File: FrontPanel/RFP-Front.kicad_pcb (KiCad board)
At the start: 2 copper layers, 106 x 56.6 mm, 21 parts, among them J1 COMM, J2 SWD, J3 BUZZ / BTNLED, U1 STM32F103C8T6, U2 OLED_128x64

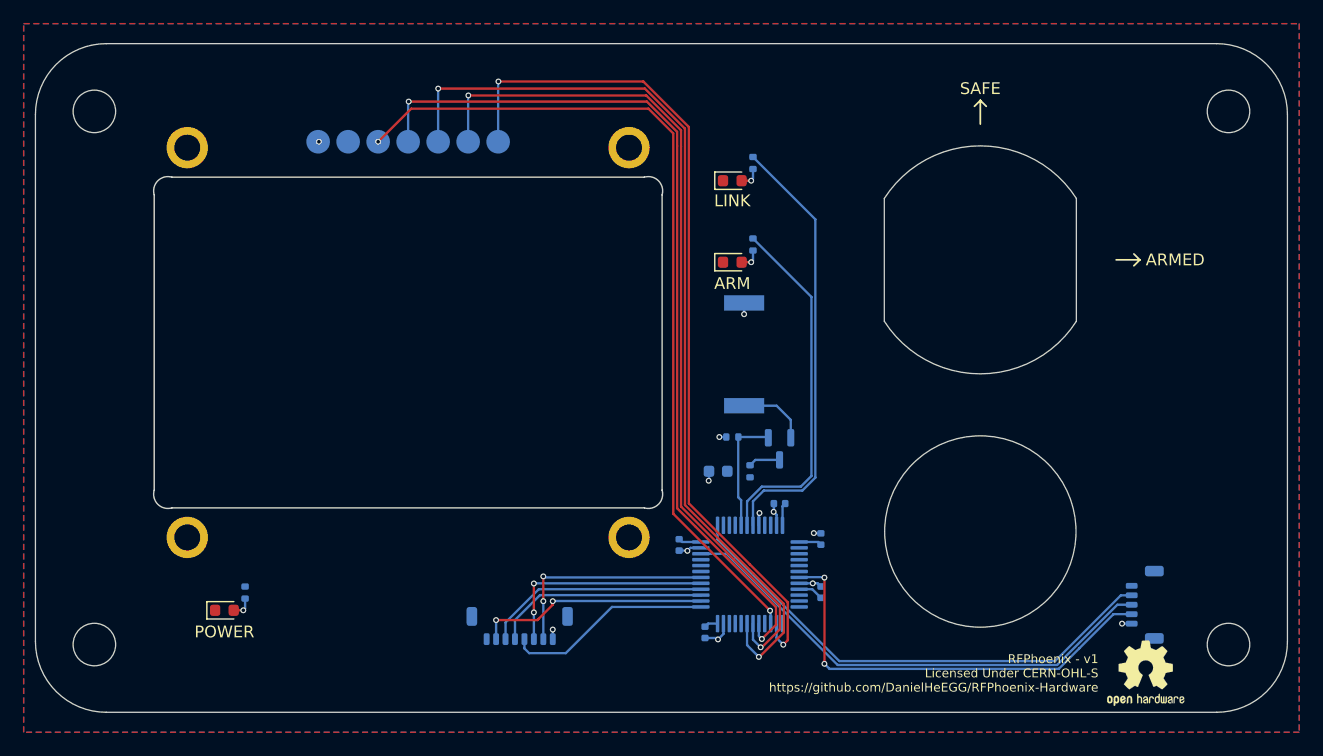
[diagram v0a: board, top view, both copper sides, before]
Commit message: Rearrange OLED and connector for front panel
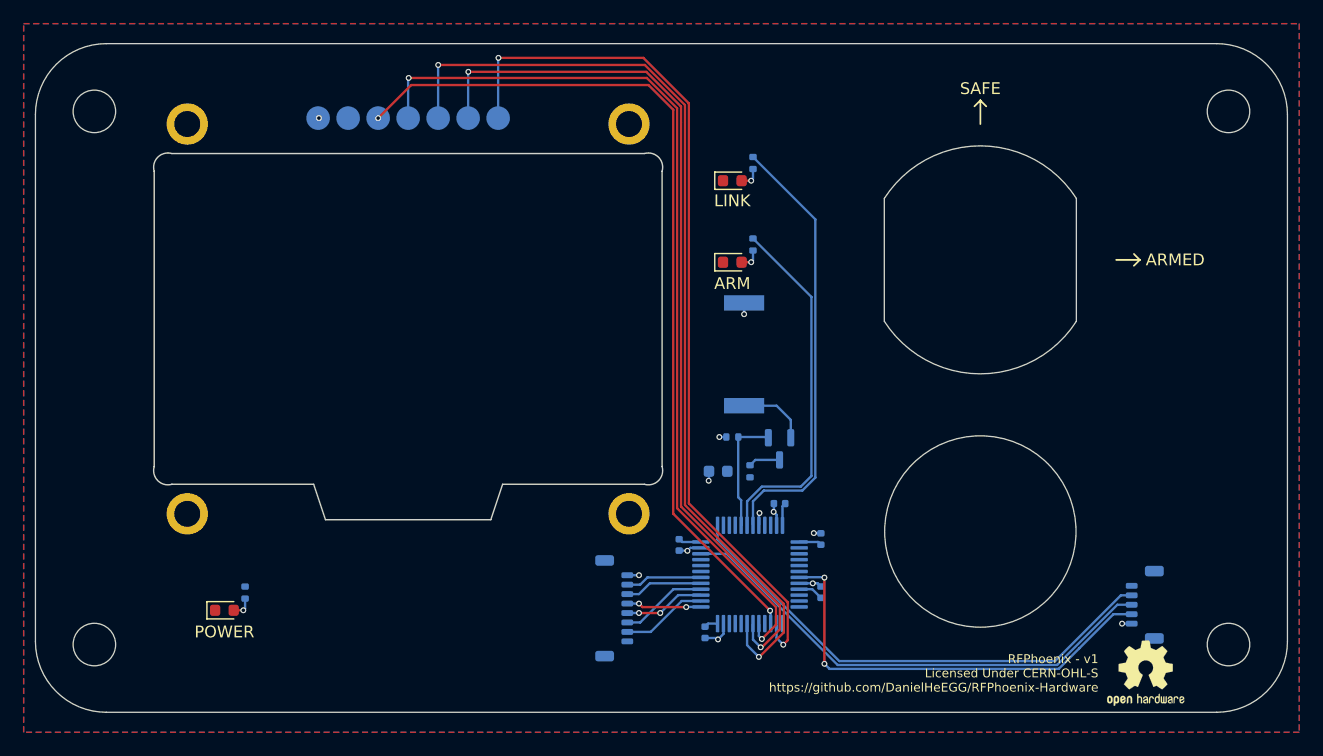
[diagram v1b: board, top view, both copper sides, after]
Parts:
- moved J1 8.14 mm to (-4.00, 19.5), turned to 90 degrees
- moved U2 2.00 mm to (-21.4, -5.00)
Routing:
- net COMM_SCK: track 19.8 -> 7.31 mm, vias 2 -> 0
- net COMM_RFU1: track 18.9 -> 6.61 mm, vias 2 -> 0
- net COMM_RFU2: track 18.7 -> 6.48 mm, vias 2 -> 0
- net COMM_MOSI: track 19.1 -> 7.39 mm
- net COMM_MISO: track 18.2 -> 6.86 mm, vias 0 -> 2
- net COMM_nCS: track 17.5 -> 6.36 mm, vias 0 -> 2
- net OLED_nCS: track 72.3 -> 74.3 mm
- net OLED_nRST: track 79.1 -> 81.1 mm
- net OLED_SCK: track 71.9 -> 73.9 mm
- net OLED_DC: track 73.4 -> 75.4 mm
- net OLED_MOSI: track 75.5 -> 77.5 mm

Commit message: Rearrange and dim LEDs
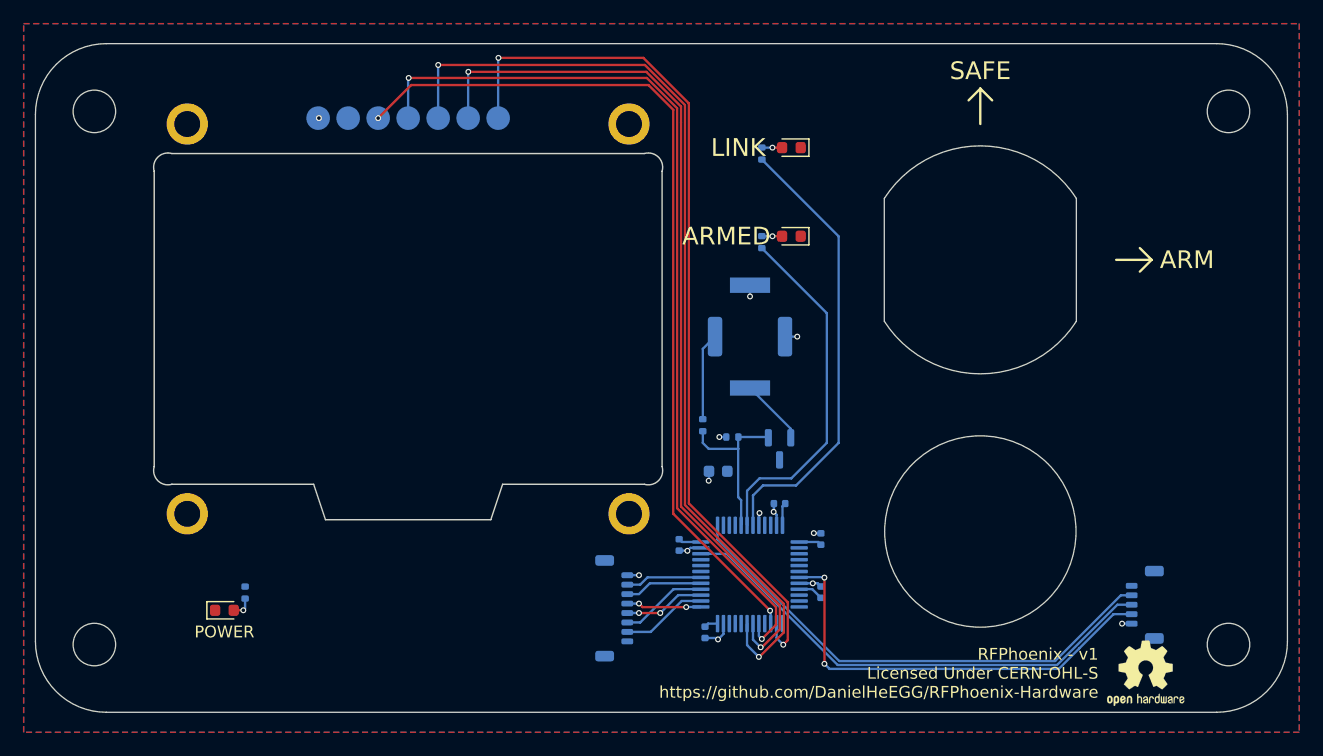
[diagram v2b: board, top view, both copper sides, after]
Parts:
- added J4: LED_LIVE, Resistor_SMD:R_2512_6332Metric, B.Cu at (7.50, -3.50)
- J3: value BUZZ / BTNLED -> BUZZER
- R1, R2: value 100 -> 470R
- R3: value 100 -> 100R
- R5: value 33 -> 100R
- moved D2 5.73 mm to (11.0, -19.5), turned to 180 degrees
- moved R5 5.59 mm to (3.50, 4.00)
- moved D3 5.46 mm to (11.0, -12.0), turned to 180 degrees
- moved J3 1.58 mm to (7.50, -3.50)
- moved R2 1.10 mm to (8.50, -19.0), turned to 90 degrees
- moved R3 0.78 mm to (8.50, -11.5), turned to 90 degrees
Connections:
- Q1 pad 3: Net-(Q1-Pad3) -> +3.3V
- R5 pad 1: +3.3V -> LED_LIVE
- R5 pad 2: Net-(Q1-Pad3) -> Net-(R5-Pad2)
- U1 pad 40: unconnected-(U1-Pad40) -> LED_CONT
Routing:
- net Net-(R5-Pad2): track 0.00 -> 7.42 mm
- net LED_LIVE: track 10.1 -> 14.3 mm
- net Net-(Q1-Pad3): track 2.69 -> 0.00 mm
- net GND: track 14.3 -> 15.4 mm, vias 12 -> 13
- net LED_LINK: track 37.5 -> 38.3 mm
